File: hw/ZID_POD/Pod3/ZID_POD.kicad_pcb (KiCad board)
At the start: 2 copper layers, 52.8 x 19.3 mm, 2 parts, among them J1 Z80-POD

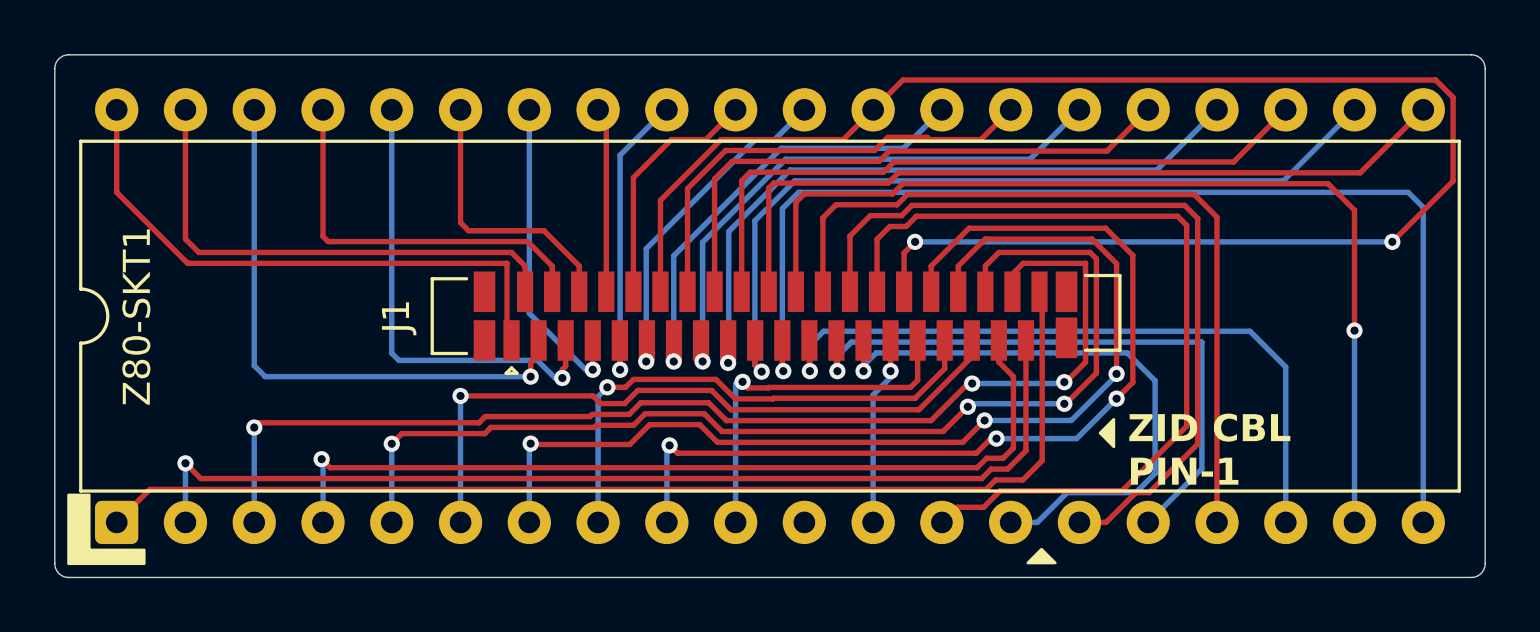
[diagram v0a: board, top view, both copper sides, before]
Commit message: POD PCB increase GND trace width
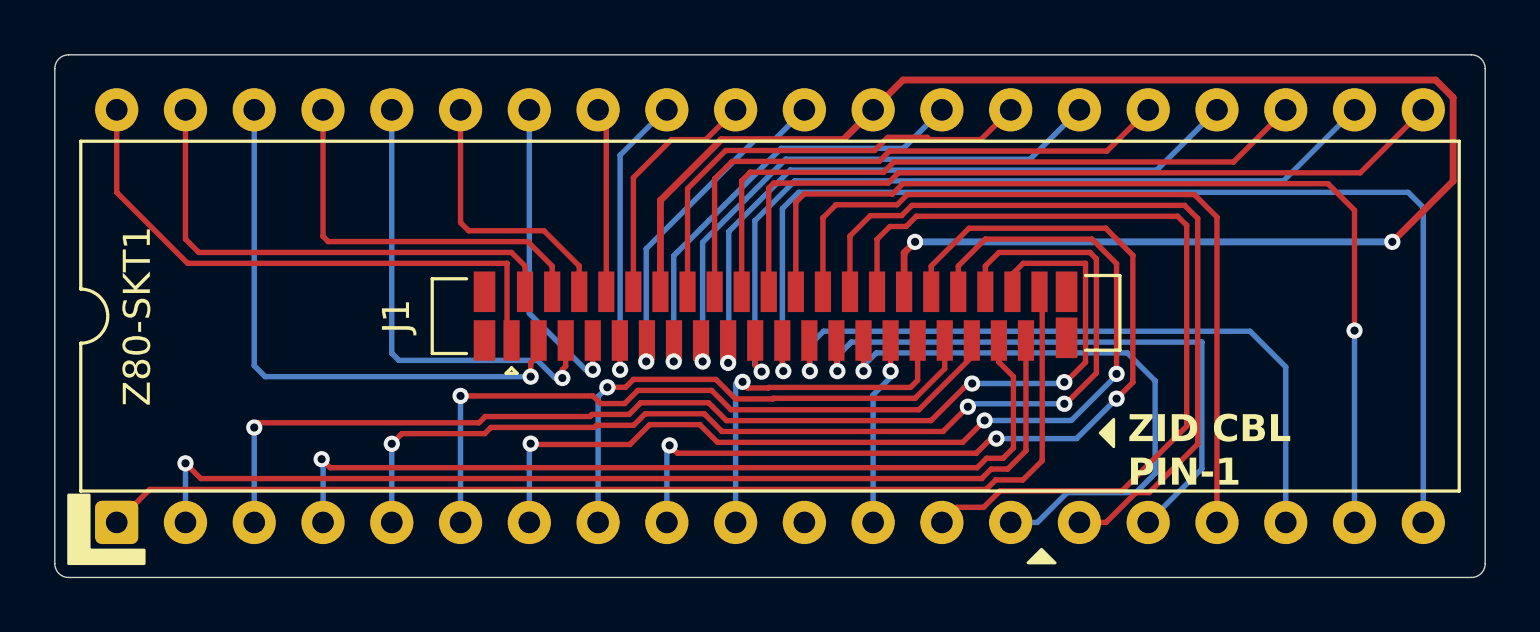
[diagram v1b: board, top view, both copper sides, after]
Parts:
- J1: value Z80-POD -> Z80-POD (3)
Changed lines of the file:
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@@
 	)
 	(setup
+		(stackup
+			(layer "F.SilkS"
+				(type "Top Silk Screen")
+			)
+			(layer "F.Paste"
+				(type "Top Solder Paste")
+			)
+			(layer "F.Mask"
+				(type "Top Solder Mask")
+				(thickness 0.01)
+			)
+			(layer "F.Cu"
+				(type "copper")
+				(thickness 0.035)
+			)
+			(layer "dielectric 1"
+				(type "core")
+				(thickness 1.51)
+				(material "FR4")
+				(epsilon_r 4.5)
+				(loss_tangent 0.02)
+			)
+			(layer "B.Cu"
+				(type "copper")
+				(thickness 0.035)
+			)
+			(layer "B.Mask"
+				(type "Bottom Solder Mask")
+				(thickness 0.01)
+			)
+			(layer "B.Paste"
+				(type "Bottom Solder Paste")
+			)
+			(layer "B.SilkS"
+				(type "Bottom Silk Screen")
+			)
+			(copper_finish "None")
+			(dielectric_constraints no)
+		)
 		(pad_to_mask_clearance 0)
 		(allow_soldermask_bridges_in_footprints no)
@@
 			)
 		)
-		(property "Value" "Z80-POD"
-			(at 0 14 90)
-			(layer "F.Fab")
+		(property "Value" "Z80-POD (3)"
+			(at 0 14 0)
+			(unlocked yes)
+			(layer "B.SilkS")
 			(effects
 				(font
@@
 					(thickness 0.15)
 				)
+				(justify mirror)
 			)
 		)
@@
 		(start 112.286 97.5771)
 		(end 114.5281 95.335)
-		(width 0.2)
+		(width 0.254)
 		(layer "F.Cu")
 		(net 3)
@@
 		(start 141.563 93.77795)
 		(end 140.91805 93.133)
-		(width 0.2)
+		(width 0.254)
 		(layer "F.Cu")
 		(net 3)
@@
 		(start 139.319 99.1108)
 		(end 141.563 96.8668)
-		(width 0.2)
+		(width 0.254)
 		(layer "F.Cu")
 		(net 3)
@@
 		(start 119.041 95.335)
 		(end 120.142 94.234)
-		(width 0.2)
+		(width 0.254)
 		(layer "F.Cu")
 		(net 3)
@@
 		(start 121.286 100.954)
 		(end 121.286 99.5162)
-		(width 0.2)
+		(width 0.254)
 		(layer "F.Cu")
 		(net 3)
@@
 		(start 140.91805 93.133)
 		(end 121.243 93.133)
-		(width 0.2)
+		(width 0.254)
 		(layer "F.Cu")
 		(net 3)
@@
 		(start 121.286 99.5162)
 		(end 121.6914 99.1108)
-		(width 0.2)
+		(width 0.254)
 		(layer "F.Cu")
 		(net 3)
@@
 		(start 114.5281 95.335)
 		(end 119.041 95.335)
-		(width 0.2)
+		(width 0.254)
 		(layer "F.Cu")
 		(net 3)
@@
 		(start 121.243 93.133)
 		(end 120.142 94.234)
-		(width 0.2)
+		(width 0.254)
 		(layer "F.Cu")
 		(net 3)
@@
 		(start 112.286 100.954)
 		(end 112.286 97.5771)
-		(width 0.2)
+		(width 0.254)
 		(layer "F.Cu")
 		(net 3)
@@
 		(start 141.563 96.8668)
 		(end 141.563 93.77795)
-		(width 0.2)
+		(width 0.254)
 		(layer "F.Cu")
 		(net 3)
@@
 		(start 121.6914 99.1108)
 		(end 139.319 99.1108)
-		(width 0.2)
+		(width 0.254)
 		(layer "B.Cu")
 		(net 3)
